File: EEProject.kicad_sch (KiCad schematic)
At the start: 3 parts, among them U1 74AHC04, U2 74AHC244, U3 74AHC244

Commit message: Devided schmetic into sub parts + ICs
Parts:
- removed U1: 74AHC04, symbol 74xx:74AHC04
- removed U2, U3: 74AHC244, symbol 74xx:74AHC244
- added U1: ATmega328-A, Package_QFP:TQFP-32_7x7mm_P0.8mm, symbol MCU_Microchip_ATmega:ATmega328-A
- added U2, U3, U4, U5: 74AHC595, symbol 74xx:74AHC595
- added U6: CP2102N-Axx-xQFN28, Package_DFN_QFN:QFN-28-1EP_5x5mm_P0.5mm_EP3.35x3.35mm, symbol Interface_USB:CP2102N-Axx-xQFN28
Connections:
- new net: U1.21 (GND), U1.3 (GND), U1.5 (GND)
- new net: U1.4 (VCC), U1.6 (VCC)
- new net: U6.29 (GND), U6.3 (GND)
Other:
- note added: "Boost Converter"
- note added: "Keyboard Data"
- note added: "Microcontroller"
- note added: "Reserved"
- note added: "UART to USB"

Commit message: Added base PCB + base schematics
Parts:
- added P1: USB_C_Plug_USB2.0, symbol Connector:USB_C_Plug_USB2.0
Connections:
- net VCC: now reaches U1.4 (VCC), U1.6 (VCC)
- net D+: now reaches U6.4 (D+)
- net D+: now also P1.A6 (D+)
- net D-: now reaches U6.5 (D-)
- net D-: now also P1.A7 (D-)
- net VBUS: now reaches U6.8 (VBUS)
- net VBUS: now also P1.A4 (VBUS), P1.A9 (VBUS), P1.B4 (VBUS), P1.B9 (VBUS)
- new net GND: P1.A1 (GND), P1.A12 (GND), P1.B1 (GND), P1.B12 (GND)
- no-connect marks 0 -> 3
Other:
- note added: "USB"
- note removed: "Reserved"

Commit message: test check
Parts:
- added U8: IR4301, Package_DFN_QFN:Infineon_PQFN-22-15-4EP_6x5mm_P0.65mm, symbol Amplifier_Audio:IR4301
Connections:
- new net: U8.15 (COM), U8.9 (COM)
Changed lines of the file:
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@@
+	)
+	(symbol
+		(lib_id "Amplifier_Audio:IR4301")
+		(at 162.56 106.68 0)
+		(unit 1)
+		(exclude_from_sim no)
+		(in_bom yes)
+		(on_board yes)
+		(dnp no)
+		(fields_autoplaced yes)
+		(property "Reference" "U8"
+			(at 169.8341 83.82 0)
+			(effects
+				(font
+					(size 1.27 1.27)
+				)
+				(justify left)
+			)
+		)
+		(property "Value" "IR4301"
+			(at 169.8341 86.36 0)
+			(effects
+				(font
+					(size 1.27 1.27)
+				)
+				(justify left)
+			)
+		)
+		(property "Footprint" "Package_DFN_QFN:Infineon_PQFN-22-15-4EP_6x5mm_P0.65mm"
+			(at 162.56 106.68 0)
+			(effects
+				(font
+					(size 1.27 1.27)
+					(italic yes)
+				)
+				(hide yes)
+			)
+		)
+		(property "Datasheet" "https://www.infineon.com/dgdl/ir4301.pdf?fileId=5546d462533600a4015355d5fc691819"
+			(at 162.56 106.68 0)
+			(effects
+				(font
+					(size 1.27 1.27)
+				)
+				(hide yes)
+			)
+		)
+		(property "Description" "PowIRaudio Integrated Analog Input Class D Audio Amplifier, 160W/4ohm, 80V, PQFN-22"
+			(at 162.56 106.68 0)
+			(effects
+				(font
+					(size 1.27 1.27)
+				)
+				(hide yes)
+			)
+		)
+		(pin "5"
+		)
+		(pin "6"
+		)
+		(pin "10"
+		)
+		(pin "12"
+		)
+		(pin "3"
+		)
+		(pin "11"
+		)
+		(pin "8"
+		)
+		(pin "1"
+		)
+		(pin "9"
+		)
+		(pin "2"
+		)
+		(pin "7"
+		)
+		(pin "14"
+		)
+		(pin "13"
+		)
+		(pin "15"
+		)
+		(pin "4"
+		)
+		(instances
+			(project ""
+				(path "/3aa1ef99-b297-42d2-a07b-7cd664ecf53c"
+					(reference "U8")
+					(unit 1)
+				)
+			)
+		)
 	)
 	(symbol

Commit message: dwa
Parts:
- added U7: IR4301, Package_DFN_QFN:Infineon_PQFN-22-15-4EP_6x5mm_P0.65mm, symbol Amplifier_Audio:IR4301
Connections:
- new net: U7.15 (COM), U7.9 (COM)
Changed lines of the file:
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@@
+		)
+	)
+	(symbol
+		(lib_id "Amplifier_Audio:IR4301")
+		(at 200.66 106.68 0)
+		(unit 1)
+		(exclude_from_sim no)
+		(in_bom yes)
+		(on_board yes)
+		(dnp no)
+		(fields_autoplaced yes)
+		(property "Reference" "U7"
+			(at 207.9341 83.82 0)
+			(effects
+				(font
+					(size 1.27 1.27)
+				)
+				(justify left)
+			)
+		)
+		(property "Value" "IR4301"
+			(at 207.9341 86.36 0)
+			(effects
+				(font
+					(size 1.27 1.27)
+				)
+				(justify left)
+			)
+		)
+		(property "Footprint" "Package_DFN_QFN:Infineon_PQFN-22-15-4EP_6x5mm_P0.65mm"
+			(at 200.66 106.68 0)
+			(effects
+				(font
+					(size 1.27 1.27)
+					(italic yes)
+				)
+				(hide yes)
+			)
+		)
+		(property "Datasheet" "https://www.infineon.com/dgdl/ir4301.pdf?fileId=5546d462533600a4015355d5fc691819"
+			(at 200.66 106.68 0)
+			(effects
+				(font
+					(size 1.27 1.27)
+				)
+				(hide yes)
+			)
+		)
+		(property "Description" "PowIRaudio Integrated Analog Input Class D Audio Amplifier, 160W/4ohm, 80V, PQFN-22"
+			(at 200.66 106.68 0)
+			(effects
+				(font
+					(size 1.27 1.27)
+				)
+				(hide yes)
+			)
+		)
+		(pin "5"
+		)
+		(pin "6"
+		)
+		(pin "10"
+		)
+		(pin "12"
+		)
+		(pin "3"
+		)
+		(pin "11"
+		)
+		(pin "8"
+		)
+		(pin "1"
+		)
+		(pin "9"
+		)
+		(pin "2"
+		)
+		(pin "7"
+		)
+		(pin "14"
+		)
+		(pin "13"
+		)
+		(pin "15"
+		)
+		(pin "4"
+		)
+		(instances
+			(project "EEProject"
+				(path "/3aa1ef99-b297-42d2-a07b-7cd664ecf53c"
+					(reference "U7")
+					(unit 1)
+				)
+			)
 		)
 	)

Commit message: Seperated Schematics
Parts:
- removed U1: ATmega328-A, Package_QFP:TQFP-32_7x7mm_P0.8mm, symbol MCU_Microchip_ATmega:ATmega328-A
- removed U2, U3, U4, U5: 74AHC595, symbol 74xx:74AHC595
- removed U6: CP2102N-Axx-xQFN28, Package_DFN_QFN:QFN-28-1EP_5x5mm_P0.5mm_EP3.35x3.35mm, symbol Interface_USB:CP2102N-Axx-xQFN28
- removed U7, U8: IR4301, Package_DFN_QFN:Infineon_PQFN-22-15-4EP_6x5mm_P0.65mm, symbol Amplifier_Audio:IR4301
- P1: footprint (none) -> Connector_USB:USB_C_Plug_Molex_105444
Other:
- added sheet Boost Converter (Boost Converter.kicad_sch)
- added sheet Keyboard Data (Keyboard Data.kicad_sch)
- added sheet Microcontroller (Microcontroller.kicad_sch)
- added sheet UART to USB (UART to USB.kicad_sch)
- note removed: "Boost Converter"
- note removed: "Keyboard Data"
- note removed: "Microcontroller"
- note removed: "UART to USB"
- note removed: "USB"
- moved on the sheet: P1

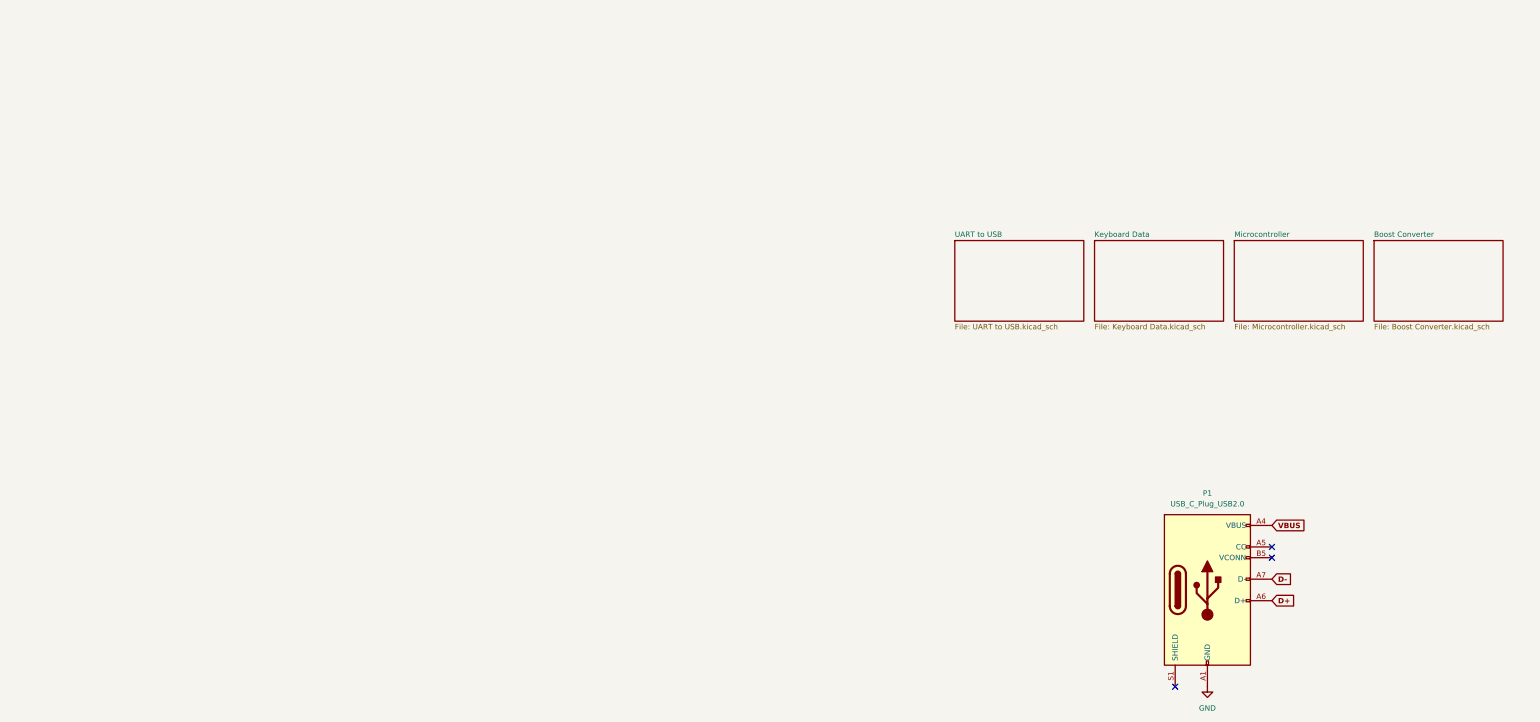
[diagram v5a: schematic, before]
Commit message: Keyboard Data Changes and added footprints
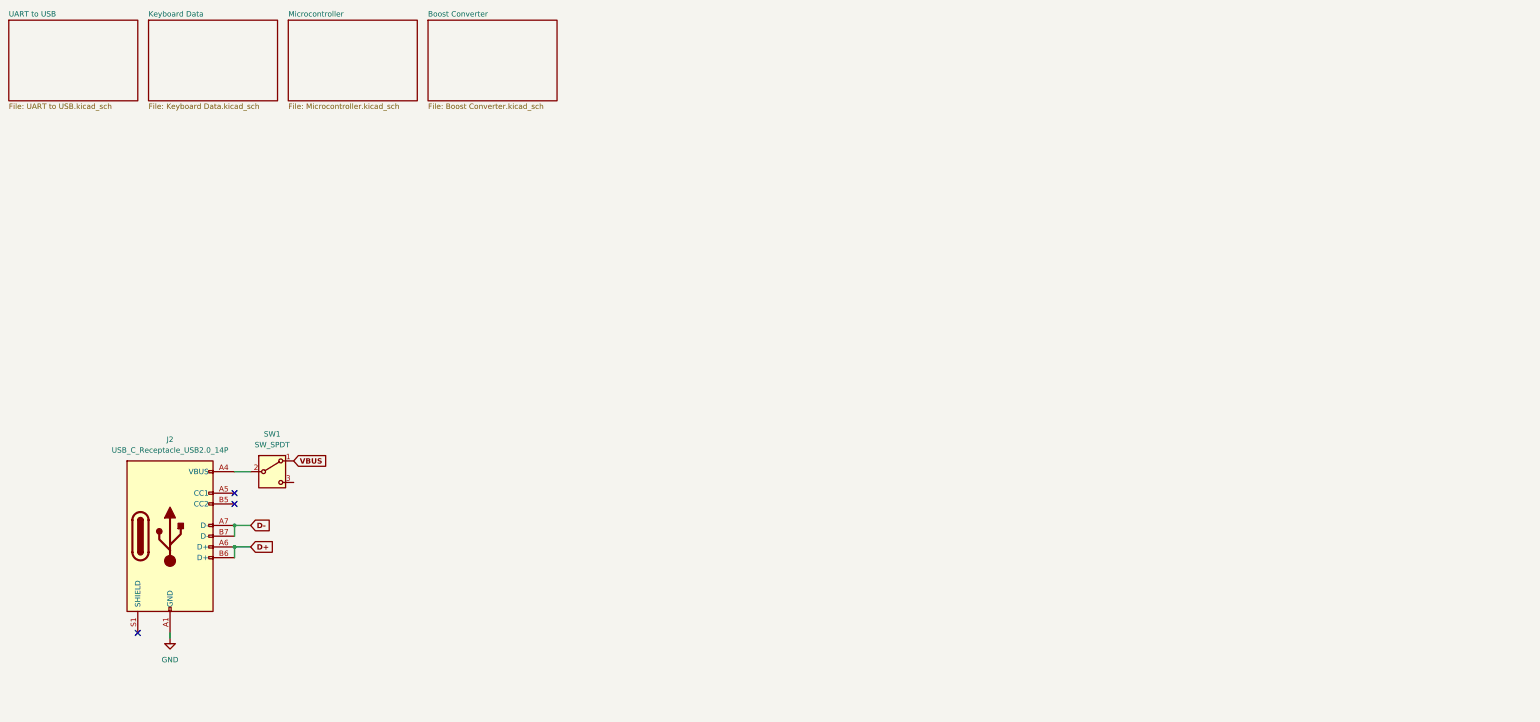
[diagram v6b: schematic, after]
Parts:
- removed P1: USB_C_Plug_USB2.0, Connector_USB:USB_C_Plug_Molex_105444, symbol Connector:USB_C_Plug_USB2.0
- added J2: USB_C_Receptacle_USB2.0_14P, Connector_USB:USB_C_Receptacle_GCT_USB4135-GF-A_6P_TopMnt_Horizontal, symbol Connector:USB_C_Receptacle_USB2.0_14P
- added SW1: SW_SPDT, Button_Switch_SMD:SW_SPDT_PCM12, symbol Switch:SW_SPDT
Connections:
- net D+: now also J2.A6 (D+), J2.B6 (D+)
- net D-: now also J2.A7 (D-), J2.B7 (D-)
- net GND: now also J2.A1 (GND), J2.A12 (GND), J2.B1 (GND), J2.B12 (GND)
- net VBUS: now also SW1.1 (A)
- new net: J2.A4 (VBUS), J2.A9 (VBUS), J2.B4 (VBUS), J2.B9 (VBUS), SW1.2 (B)
